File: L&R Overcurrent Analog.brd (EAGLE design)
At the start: 55 x 72.5 mm, 22 parts, among them IC1 TLC393CPN, IC2 CSLA2CFTH, Q1 SUP75P0307, Q2 SUP75P0307, X1 J1, X2 J2, X3 J3

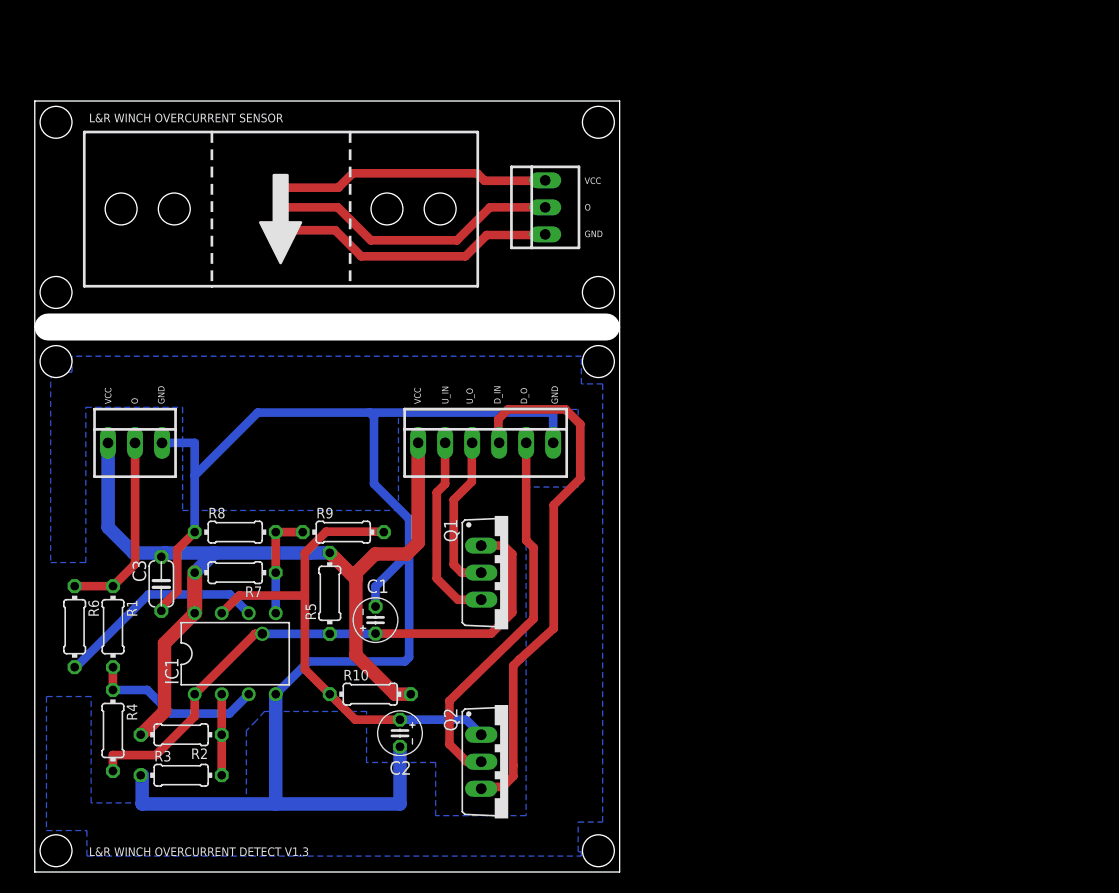
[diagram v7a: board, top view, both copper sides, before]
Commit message: Updated board dimensions, added BOM
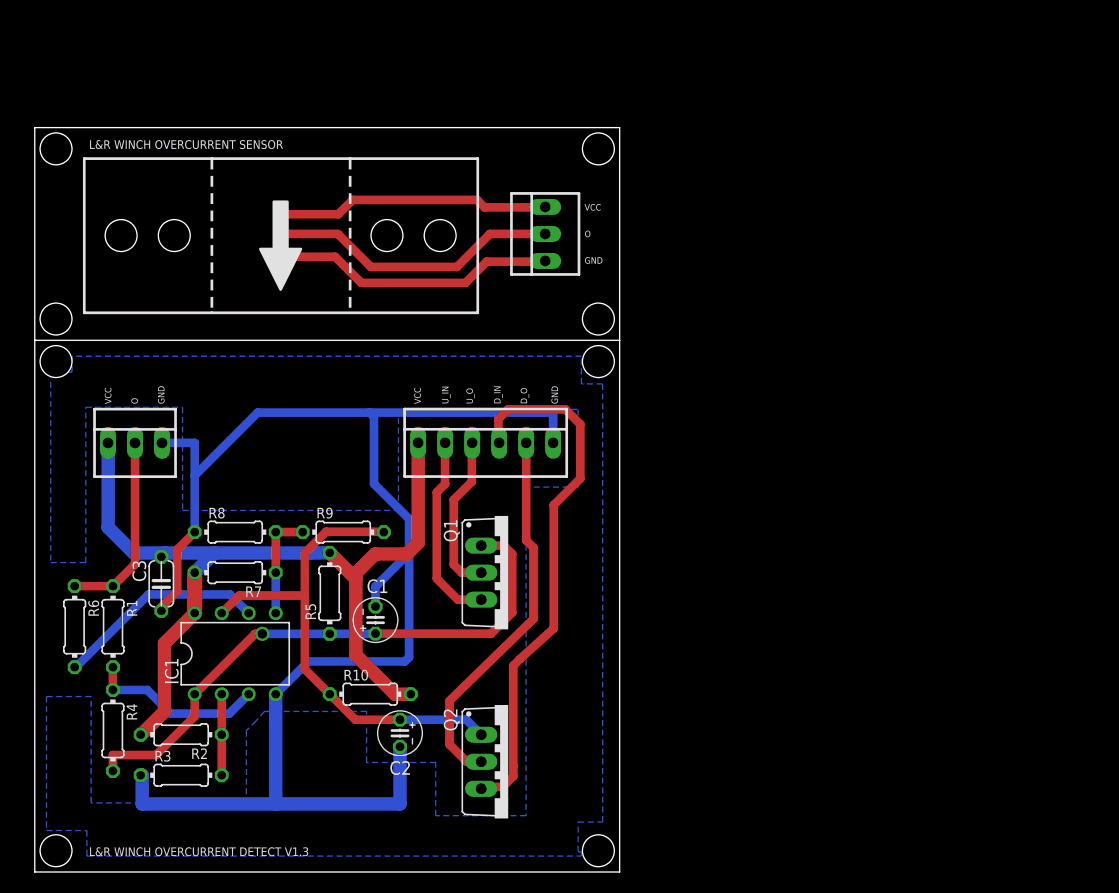
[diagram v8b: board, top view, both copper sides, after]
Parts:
- moved IC2 2.50 mm to (23.1, 59.9)
- moved X3 2.50 mm to (48.0, 60.0)
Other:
- board size 55 x 72.5 mm -> 55 x 70 mm
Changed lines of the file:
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@@
 <plain>
 <wire x1="0" y1="0" x2="55" y2="0" width="0" layer="20"/>
-<wire x1="55" y1="0" x2="55" y2="51.25" width="0" layer="20"/>
-<wire x1="0" y1="51.25" x2="0" y2="0" width="0" layer="20"/>
+<wire x1="55" y1="0" x2="55" y2="50" width="0" layer="20"/>
 <text x="5.1" y="1.5" size="0.8128" layer="21">L&amp;R WINCH OVERCURRENT DETECT V1.3</text>
 <text x="36.3" y="44" size="0.6096" layer="21" rot="R90">VCC</text>
@@
 <hole x="2" y="48" drill="3"/>
 <hole x="53" y="48" drill="3"/>
-<wire x1="55" y1="72.5" x2="0" y2="72.5" width="0" layer="20"/>
-<wire x1="55" y1="72.5" x2="55" y2="51.25" width="0" layer="20"/>
-<wire x1="0" y1="72.5" x2="0" y2="51.25" width="0" layer="20"/>
-<hole x="2" y="54.5" drill="3"/>
-<hole x="2" y="70.5" drill="3"/>
-<hole x="53" y="70.5" drill="3"/>
-<hole x="53" y="54.5" drill="3"/>
+<wire x1="0" y1="50" x2="0" y2="0" width="0" layer="20"/>
+<wire x1="55" y1="70" x2="0" y2="70" width="0" layer="20"/>
+<wire x1="55" y1="70" x2="55" y2="50" width="0" layer="20"/>
+<wire x1="0" y1="70" x2="0" y2="50" width="0" layer="20"/>
+<hole x="2" y="52" drill="3"/>
+<hole x="2" y="68" drill="3"/>
+<hole x="53" y="68" drill="3"/>
+<hole x="53" y="52" drill="3"/>
 <text x="7.2" y="44" size="0.6096" layer="21" rot="R90">VCC</text>
 <text x="9.7" y="44" size="0.6096" layer="21" rot="R90">O</text>
 <text x="12.2" y="44" size="0.6096" layer="21" rot="R90">GND</text>
-<text x="51.7" y="64.7" size="0.6096" layer="21">VCC</text>
-<text x="51.7" y="62.2" size="0.6096" layer="21">O</text>
-<text x="51.7" y="59.7" size="0.6096" layer="21">GND</text>
+<text x="51.7" y="62.2" size="0.6096" layer="21">VCC</text>
+<text x="51.7" y="59.7" size="0.6096" layer="21">O</text>
+<text x="51.7" y="57.2" size="0.6096" layer="21">GND</text>
 <text x="63.5" y="-53.34" size="2.54" layer="48">CURRENT LIMIT BOARD FOR SIDE LAUNCH
 AND RECOVERY WINCH.</text>
@@
 <text x="152.4" y="-71.755" size="2.54" layer="48">v1.3</text>
 <text x="152.4" y="-77.724" size="2.54" layer="48">1/1</text>
-<text x="5.1" y="70.5" size="0.8128" layer="21">L&amp;R WINCH OVERCURRENT SENSOR</text>
-<wire x1="53.75" y1="51.25" x2="1.25" y2="51.25" width="2.54" layer="20"/>
+<text x="5.1" y="68" size="0.8128" layer="21">L&amp;R WINCH OVERCURRENT SENSOR</text>
+<wire x1="55" y1="50" x2="0" y2="50" width="0" layer="20"/>
 </plain>
 <attributes>
@@
 </autorouter>
 <elements>
-<element name="IC2" library="Overcurrent Detect" package="CSLA2CF" value="CSLA2CFTH" x="23.12" y="62.35" smashed="yes"/>
+<element name="IC2" library="Overcurrent Detect" package="CSLA2CF" value="CSLA2CFTH" x="23.12" y="59.85" smashed="yes"/>
 <element name="IC1" library="Overcurrent Detect" package="DIL08" value="TLC393CPN" x="18.85" y="20.53" smashed="yes">
 <attribute name="NAME" x="13.516" y="17.609" size="1.27" layer="25" ratio="10" rot="R90"/>
@@
 <attribute name="OC_FARNELL" value="1462950" x="9.4282625" y="40.350846875" size="1.778" layer="27" display="off"/>
 </element>
-<element name="X3" library="Overcurrent Detect" package="22-23-2031" value="J3" x="48" y="62.5" smashed="yes" rot="R90">
-<attribute name="OC_NEWARK" value="30C0862" x="48" y="62.5" size="1.778" layer="27" rot="R90" display="off"/>
-<attribute name="MPN" value="22-23-2031" x="48" y="62.5" size="1.778" layer="27" rot="R90" display="off"/>
-<attribute name="MF" value="MOLEX" x="48" y="62.5" size="1.778" layer="27" rot="R90" display="off"/>
-<attribute name="OC_FARNELL" value="1462950" x="48" y="62.5" size="1.778" layer="27" rot="R90" display="off"/>
+<element name="X3" library="Overcurrent Detect" package="22-23-2031" value="J3" x="48" y="60" smashed="yes" rot="R90">
+<attribute name="OC_NEWARK" value="30C0862" x="48" y="60" size="1.778" layer="27" rot="R90" display="off"/>
+<attribute name="MPN" value="22-23-2031" x="48" y="60" size="1.778" layer="27" rot="R90" display="off"/>
+<attribute name="MF" value="MOLEX" x="48" y="60" size="1.778" layer="27" rot="R90" display="off"/>
+<attribute name="OC_FARNELL" value="1462950" x="48" y="60" size="1.778" layer="27" rot="R90" display="off"/>
 </element>
 <element name="FRAME1" library="L&amp;R Overcurrent Analog" package="FRAME_A_L" value="" x="-112.51" y="-79.09"/>
@@
 <contactref element="IC2" pad="V+"/>
 <contactref element="X3" pad="1"/>
-<wire x1="23.12" y1="60.35" x2="28.25" y2="60.35" width="0.8128" layer="1"/>
-<wire x1="28.25" y1="60.35" x2="30.7" y2="57.9" width="0.8128" layer="1"/>
-<wire x1="30.7" y1="57.9" x2="40.5" y2="57.9" width="0.8128" layer="1"/>
-<wire x1="40.5" y1="57.9" x2="42.5" y2="59.9" width="0.8128" layer="1"/>
-<wire x1="42.5" y1="59.9" x2="47.94" y2="59.9" width="0.8128" layer="1"/>
-<wire x1="47.94" y1="59.9" x2="48" y2="59.96" width="0.8128" layer="1"/>
+<wire x1="23.12" y1="57.85" x2="28.25" y2="57.85" width="0.8128" layer="1"/>
+<wire x1="28.25" y1="57.85" x2="30.7" y2="55.4" width="0.8128" layer="1"/>
+<wire x1="30.7" y1="55.4" x2="40.5" y2="55.4" width="0.8128" layer="1"/>
+<wire x1="40.5" y1="55.4" x2="42.5" y2="57.4" width="0.8128" layer="1"/>
+<wire x1="42.5" y1="57.4" x2="47.94" y2="57.4" width="0.8128" layer="1"/>
+<wire x1="47.94" y1="57.4" x2="48" y2="57.46" width="0.8128" layer="1"/>
 </signal>
 <signal name="N$13">
 <contactref element="IC2" pad="V-"/>
 <contactref element="X3" pad="3"/>
-<wire x1="23.12" y1="64.35" x2="28.55" y2="64.35" width="0.8128" layer="1"/>
-<wire x1="28.55" y1="64.35" x2="29.9" y2="65.7" width="0.8128" layer="1"/>
-<wire x1="29.9" y1="65.7" x2="41.6" y2="65.7" width="0.8128" layer="1"/>
-<wire x1="41.6" y1="65.7" x2="42.3" y2="65" width="0.8128" layer="1"/>
-<wire x1="42.3" y1="65" x2="47.96" y2="65" width="0.8128" layer="1"/>
-<wire x1="47.96" y1="65" x2="48" y2="65.04" width="0.8128" layer="1"/>
+<wire x1="23.12" y1="61.85" x2="28.55" y2="61.85" width="0.8128" layer="1"/>
+<wire x1="28.55" y1="61.85" x2="29.9" y2="63.2" width="0.8128" layer="1"/>
+<wire x1="29.9" y1="63.2" x2="41.6" y2="63.2" width="0.8128" layer="1"/>
+<wire x1="41.6" y1="63.2" x2="42.3" y2="62.5" width="0.8128" layer="1"/>
+<wire x1="42.3" y1="62.5" x2="47.96" y2="62.5" width="0.8128" layer="1"/>
+<wire x1="47.96" y1="62.5" x2="48" y2="62.54" width="0.8128" layer="1"/>
 </signal>
 <signal name="N$14">
 <contactref element="IC2" pad="O"/>
 <contactref element="X3" pad="2"/>
-<wire x1="23.27" y1="62.5" x2="23.12" y2="62.35" width="0.8128" layer="1"/>
-<wire x1="23.27" y1="62.5" x2="28.5" y2="62.5" width="0.8128" layer="1"/>
-<wire x1="28.5" y1="62.5" x2="31.6" y2="59.4" width="0.8128" layer="1"/>
-<wire x1="31.6" y1="59.4" x2="39.7" y2="59.4" width="0.8128" layer="1"/>
-<wire x1="39.7" y1="59.4" x2="42.8" y2="62.5" width="0.8128" layer="1"/>
-<wire x1="42.8" y1="62.5" x2="48" y2="62.5" width="0.8128" layer="1"/>
+<wire x1="23.27" y1="60" x2="23.12" y2="59.85" width="0.8128" layer="1"/>
+<wire x1="23.27" y1="60" x2="28.5" y2="60" width="0.8128" layer="1"/>
+<wire x1="28.5" y1="60" x2="31.6" y2="56.9" width="0.8128" layer="1"/>
+<wire x1="31.6" y1="56.9" x2="39.7" y2="56.9" width="0.8128" layer="1"/>
+<wire x1="39.7" y1="56.9" x2="42.8" y2="60" width="0.8128" layer="1"/>
+<wire x1="42.8" y1="60" x2="48" y2="60" width="0.8128" layer="1"/>
 </signal>
 <signal name="N$15">
